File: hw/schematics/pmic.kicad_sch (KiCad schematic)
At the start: 40 parts, among them J1 TYPE-C-31-M-13C, J2 Conn_01x02, U1 NPM1300-QEAA-R

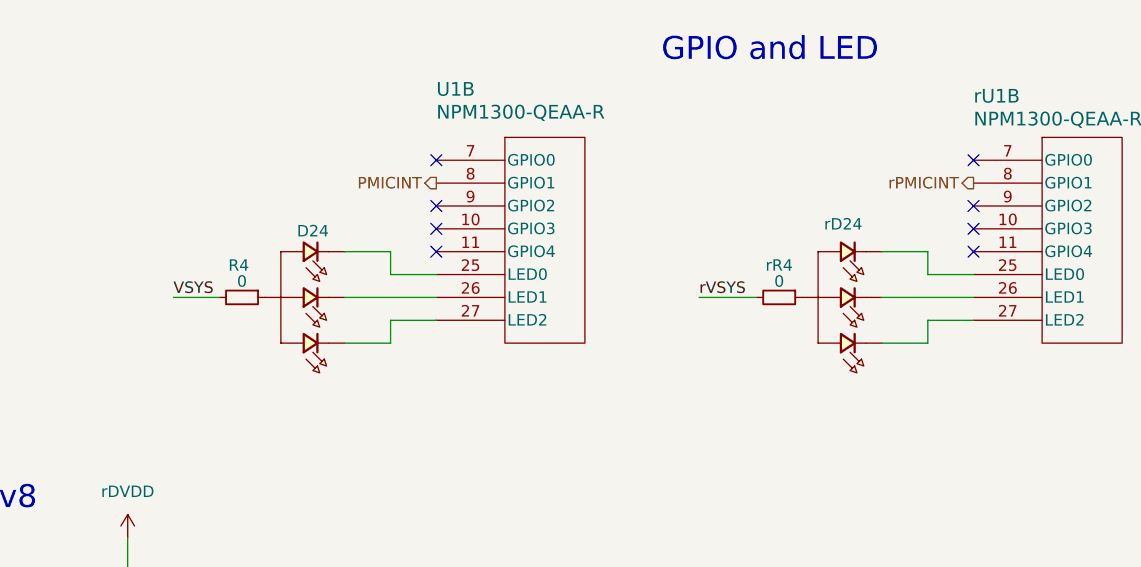
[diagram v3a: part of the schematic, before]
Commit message: Add extra pmic gpios
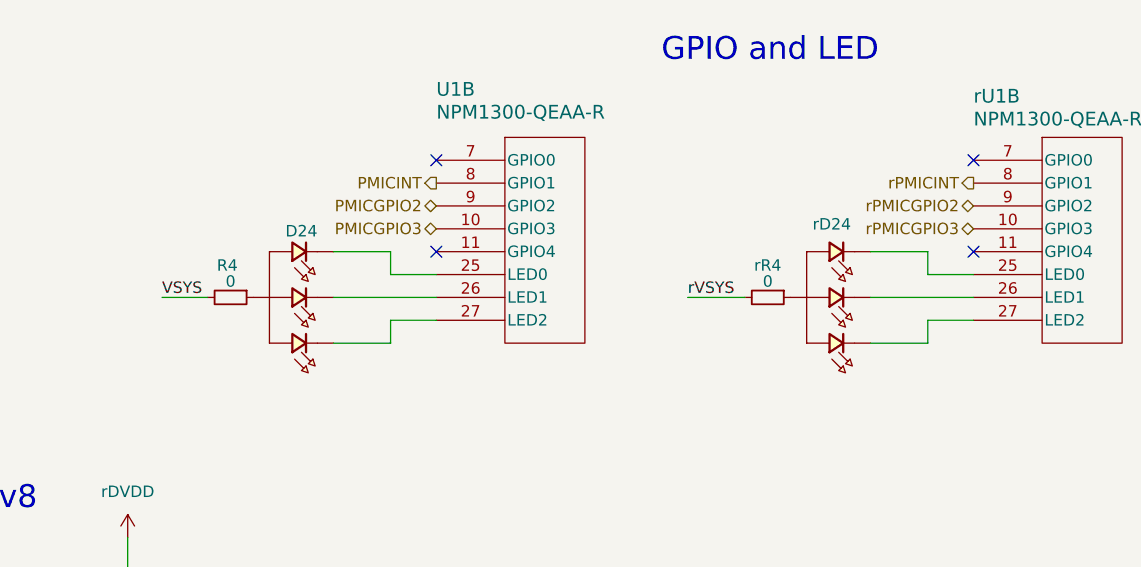
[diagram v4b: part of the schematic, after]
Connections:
- net PMICGPIO3: now reaches U1.10 (GPIO3)
- net PMICGPIO2: now reaches U1.9 (GPIO2)
- net rPMICGPIO3: now reaches rU1.10 (GPIO3)
- net rPMICGPIO2: now reaches rU1.9 (GPIO2)
- no-connect marks 28 -> 24
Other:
- moved on the sheet: D24, R4, rD24, rR4
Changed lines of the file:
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@@
 	)
 	(no_connect
-		(at 295.91 177.8)
-	)
-	(no_connect
 		(at 181.61 68.58)
 	)
@@
 	)
 	(no_connect
-		(at 295.91 175.26)
-	)
-	(no_connect
 		(at 181.61 60.96)
 	)
@@
 	)
 	(no_connect
-		(at 355.6 177.8)
-	)
-	(no_connect
-		(at 355.6 175.26)
-	)
-	(no_connect
 		(at 76.2 67.31)
 	)
@@
 	(wire
 		(pts
-			(xy 350.52 180.34) (xy 345.44 180.34)
+			(xy 350.52 180.34) (xy 344.17 180.34)
 		)
 		(stroke
@@
 	(wire
 		(pts
-			(xy 266.7 185.42) (xy 271.78 185.42)
+			(xy 265.43 185.42) (xy 270.51 185.42)
 		)
 		(stroke
@@
 	(wire
 		(pts
-			(xy 285.75 185.42) (xy 295.91 185.42)
+			(xy 284.48 185.42) (xy 295.91 185.42)
 		)
 		(stroke
@@
 	(wire
 		(pts
-			(xy 345.44 185.42) (xy 355.6 185.42)
+			(xy 344.17 185.42) (xy 355.6 185.42)
 		)
 		(stroke
@@
 	(wire
 		(pts
-			(xy 325.12 185.42) (xy 331.47 185.42)
+			(xy 323.85 185.42) (xy 330.2 185.42)
 		)
 		(stroke
@@
 	(wire
 		(pts
-			(xy 290.83 190.5) (xy 285.75 190.5)
+			(xy 290.83 190.5) (xy 284.48 190.5)
 		)
 		(stroke
@@
 	(wire
 		(pts
-			(xy 350.52 190.5) (xy 345.44 190.5)
+			(xy 350.52 190.5) (xy 344.17 190.5)
 		)
 		(stroke
@@
 	(wire
 		(pts
-			(xy 290.83 180.34) (xy 285.75 180.34)
+			(xy 290.83 180.34) (xy 284.48 180.34)
 		)
 		(stroke
@@
 	)
 	(label "VSYS"
-		(at 266.7 185.42 0)
+		(at 265.43 185.42 0)
 		(effects
 			(font
@@
 	)
 	(label "rVSYS"
-		(at 325.12 185.42 0)
+		(at 323.85 185.42 0)
 		(effects
 			(font
@@
 		)
 	)
+	(hierarchical_label "PMICGPIO2"
+		(shape bidirectional)
+		(at 295.91 175.26 180)
+		(effects
+			(font
+				(size 1.27 1.27)
+			)
+			(justify right)
+		)
+	)
 	(hierarchical_label "rPMICINT"
 		(shape output)
@@
 		)
 	)
+	(hierarchical_label "PMICGPIO3"
+		(shape bidirectional)
+		(at 295.91 177.8 180)
+		(effects
+			(font
+				(size 1.27 1.27)
+			)
+			(justify right)
+		)
+	)
 	(hierarchical_label "rSDA"
 		(shape bidirectional)
@@
 		)
 	)
+	(hierarchical_label "rPMICGPIO2"
+		(shape bidirectional)
+		(at 355.6 175.26 180)
+		(effects
+			(font
+				(size 1.27 1.27)
+			)
+			(justify right)
+		)
+	)
+	(hierarchical_label "rPMICGPIO3"
+		(shape bidirectional)
+		(at 355.6 177.8 180)
+		(effects
+			(font
+				(size 1.27 1.27)
+			)
+			(justify right)
+		)
+	)
 	(hierarchical_label "SCL"
 		(shape input)
@@
 	(symbol
 		(lib_id "Alidade:LED_RGB_COM_ANODE")
-		(at 341.63 185.42 0)
+		(at 340.36 185.42 0)
 		(mirror y)
 		(unit 1)
@@
 		(dnp no)
 		(property "Reference" "rD24"
-			(at 341.122 177.292 0)
+			(at 339.852 177.292 0)
 			(effects
 				(font
@@
 		)
 		(property "Value" "LED_RGB_COM_ANODE"
-			(at 340.995 176.53 0)
+			(at 339.725 176.53 0)
 			(effects
 				(font
@@
 		)
 		(property "Footprint" ""
-			(at 341.63 185.42 90)
+			(at 340.36 185.42 90)
 			(effects
 				(font
@@
 		)
 		(property "Datasheet" ""
-			(at 341.63 185.42 90)
+			(at 340.36 185.42 90)
 			(effects
 				(font
@@
 		)
 		(property "Description" ""
-			(at 341.63 185.42 0)
+			(at 340.36 185.42 0)
 			(effects
 				(font
@@
 	(symbol
 		(lib_id "Alidade:R")
-		(at 274.32 185.42 270)
+		(at 273.05 185.42 270)
 		(unit 1)
 		(exclude_from_sim no)
@@
 		(dnp no)
 		(property "Reference" "R4"
-			(at 272.796 181.864 90)
+			(at 271.526 181.864 90)
 			(effects
 				(font
@@
 		)
 		(property "Value" "0"
-			(at 274.32 183.642 90)
+			(at 273.05 183.642 90)
 			(do_not_autoplace yes)
 			(effects
@@
 		)
 		(property "Footprint" "Alidade:0603"
-			(at 274.32 185.42 0)
+			(at 273.05 185.42 0)
 			(effects
 				(font
@@
 		)
 		(property "Datasheet" ""
-			(at 274.32 185.42 0)
+			(at 273.05 185.42 0)
 			(effects
 				(font
@@
 		)
 		(property "Description" ""
-			(at 274.32 185.42 0)
+			(at 273.05 185.42 0)
 			(effects
 				(font
@@
 		)
 		(property "LCSC Part #" "C21189"
-			(at 274.32 185.42 90)
+			(at 273.05 185.42 90)
 			(effects
 				(font
@@
 	(symbol
 		(lib_id "Alidade:R")
-		(at 334.01 185.42 270)
+		(at 332.74 185.42 270)
 		(unit 1)
 		(exclude_from_sim no)
@@
 		(dnp no)
 		(property "Reference" "rR4"
-			(at 332.486 181.864 90)
+			(at 331.216 181.864 90)
 			(effects
 				(font
@@
 		)
 		(property "Value" "0"
-			(at 334.01 183.642 90)
+			(at 332.74 183.642 90)
 			(do_not_autoplace yes)
 			(effects
@@
 		)
 		(property "Footprint" "Alidade:0603"
-			(at 334.01 185.42 0)
+			(at 332.74 185.42 0)
 			(effects
 				(font
@@
 		)
 		(property "Datasheet" ""
-			(at 334.01 185.42 0)
+			(at 332.74 185.42 0)
 			(effects
 				(font
@@
 		)
 		(property "Description" ""
-			(at 334.01 185.42 0)
+			(at 332.74 185.42 0)
 			(effects
 				(font
@@
 		)
 		(property "LCSC Part #" "C21189"
-			(at 334.01 185.42 90)
+			(at 332.74 185.42 90)
 			(effects
 				(font
@@
 	(symbol
 		(lib_id "Alidade:LED_RGB_COM_ANODE")
-		(at 281.94 185.42 0)
+		(at 280.67 185.42 0)
 		(mirror y)
 		(unit 1)
@@
 		(dnp no)
 		(property "Reference" "D24"
-			(at 282.194 178.054 0)
+			(at 280.924 178.054 0)
 			(effects
 				(font
@@
 		)
 		(property "Value" "LED_RGB_COM_ANODE"
-			(at 281.305 176.53 0)
+			(at 280.035 176.53 0)
 			(effects
 				(font
@@
 		)
 		(property "Footprint" ""
-			(at 281.94 185.42 90)
+			(at 280.67 185.42 90)
 			(effects
 				(font
@@
 		)
 		(property "Datasheet" ""
-			(at 281.94 185.42 90)
+			(at 280.67 185.42 90)
 			(effects
 				(font
@@
 		)
 		(property "Description" ""
-			(at 281.94 185.42 0)
+			(at 280.67 185.42 0)
 			(effects
 				(font

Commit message: Add a bunch of models and footprints
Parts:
- C1, C2, C3, C4, C5, C6, C7, C8, rC1, rC2, rC3, rC4, rC5, rC6, rC7, rC8: footprint Alidade:0603 -> Alidade:C_0603_1608Metric
- L1, L2, rL1, rL2: footprint Alidade:0603 -> Alidade:L_0603_1608Metric
- R1, R2, R3, R4, R5, R6, rR1, rR2, rR3, rR4, rR5, rR6: footprint Alidade:0603 -> Alidade:R_0603_1608Metric
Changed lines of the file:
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@@
 			)
 		)
-		(property "Footprint" "Alidade:0603"
+		(property "Footprint" "Alidade:L_0603_1608Metric"
 			(at 43.18 143.51 0)
 			(effects
@@
 			)
 		)
-		(property "Footprint" "Alidade:0603"
+		(property "Footprint" "Alidade:R_0603_1608Metric"
 			(at 182.88 220.98 0)
 			(effects
@@
 			)
 		)
-		(property "Footprint" "Alidade:0603"
+		(property "Footprint" "Alidade:L_0603_1608Metric"
 			(at 138.43 147.32 0)
 			(effects
@@
 			)
 		)
-		(property "Footprint" "Alidade:0603"
+		(property "Footprint" "Alidade:C_0603_1608Metric"
 			(at 350.52 133.35 0)
 			(effects
@@
 			)
 		)
-		(property "Footprint" "Alidade:0603"
+		(property "Footprint" "Alidade:R_0603_1608Metric"
 			(at 356.87 69.85 0)
 			(effects
@@
 			)
 		)
-		(property "Footprint" "Alidade:0603"
+		(property "Footprint" "Alidade:C_0603_1608Metric"
 			(at 335.28 133.35 0)
 			(effects
@@
 			)
 		)
-		(property "Footprint" "Alidade:0603"
+		(property "Footprint" "Alidade:C_0603_1608Metric"
 			(at 279.4 133.35 0)
 			(effects
@@
 			)
 		)
-		(property "Footprint" "Alidade:0603"
+		(property "Footprint" "Alidade:C_0603_1608Metric"
 			(at 347.98 73.66 0)
 			(effects
@@
 			)
 		)
-		(property "Footprint" "Alidade:0603"
+		(property "Footprint" "Alidade:C_0603_1608Metric"
 			(at 264.16 133.35 0)
 			(effects
@@
 			)
 		)
-		(property "Footprint" "Alidade:0603"
+		(property "Footprint" "Alidade:C_0603_1608Metric"
 			(at 256.54 133.35 0)
 			(effects
@@
 			)
 		)
-		(property "Footprint" "Alidade:0603"
+		(property "Footprint" "Alidade:R_0603_1608Metric"
 			(at 285.75 68.58 0)
 			(effects
@@
 			)
 		)
-		(property "Footprint" "Alidade:0603"
+		(property "Footprint" "Alidade:R_0603_1608Metric"
 			(at 176.53 220.98 0)
 			(effects
@@
 			)
 		)
-		(property "Footprint" "Alidade:0603"
+		(property "Footprint" "Alidade:R_0603_1608Metric"
 			(at 142.24 153.67 0)
 			(effects
@@
 			)
 		)
-		(property "Footprint" "Alidade:0603"
+		(property "Footprint" "Alidade:R_0603_1608Metric"
 			(at 46.99 149.86 0)
 			(effects
@@
 			)
 		)
-		(property "Footprint" "Alidade:0603"
+		(property "Footprint" "Alidade:R_0603_1608Metric"
 			(at 273.05 185.42 0)
 			(effects
@@
 			)
 		)
-		(property "Footprint" "Alidade:0603"
+		(property "Footprint" "Alidade:R_0603_1608Metric"
 			(at 87.63 148.59 0)
 			(effects
@@
 			)
 		)
-		(property "Footprint" "Alidade:0603"
+		(property "Footprint" "Alidade:C_0603_1608Metric"
 			(at 81.28 60.96 0)
 			(effects
@@
 			)
 		)
-		(property "Footprint" "Alidade:0603"
+		(property "Footprint" "Alidade:C_0603_1608Metric"
 			(at 133.35 153.67 0)
 			(effects
@@
 			)
 		)
-		(property "Footprint" "Alidade:0603"
+		(property "Footprint" "Alidade:R_0603_1608Metric"
 			(at 250.19 222.25 0)
 			(effects
@@
 			)
 		)
-		(property "Footprint" "Alidade:0603"
+		(property "Footprint" "Alidade:L_0603_1608Metric"
 			(at 83.82 142.24 0)
 			(effects
@@
 			)
 		)
-		(property "Footprint" "Alidade:0603"
+		(property "Footprint" "Alidade:R_0603_1608Metric"
 			(at 332.74 185.42 0)
 			(effects
@@
 			)
 		)
-		(property "Footprint" "Alidade:0603"
+		(property "Footprint" "Alidade:C_0603_1608Metric"
 			(at 38.1 149.86 0)
 			(effects
@@
 			)
 		)
-		(property "Footprint" "Alidade:0603"
+		(property "Footprint" "Alidade:L_0603_1608Metric"
 			(at 181.61 146.05 0)
 			(effects
@@
 			)
 		)
-		(property "Footprint" "Alidade:0603"
+		(property "Footprint" "Alidade:C_0603_1608Metric"
 			(at 78.74 148.59 0)
 			(effects
@@
 			)
 		)
-		(property "Footprint" "Alidade:0603"
+		(property "Footprint" "Alidade:R_0603_1608Metric"
 			(at 256.54 222.25 0)
 			(effects
@@
 			)
 		)
-		(property "Footprint" "Alidade:0603"
+		(property "Footprint" "Alidade:C_0603_1608Metric"
 			(at 327.66 133.35 0)
 			(effects
@@
 			)
 		)
-		(property "Footprint" "Alidade:0603"
+		(property "Footprint" "Alidade:R_0603_1608Metric"
 			(at 185.42 152.4 0)
 			(effects
@@
 			)
 		)
-		(property "Footprint" "Alidade:0603"
+		(property "Footprint" "Alidade:C_0603_1608Metric"
 			(at 271.78 133.35 0)
 			(effects
@@
 			)
 		)
-		(property "Footprint" "Alidade:0603"
+		(property "Footprint" "Alidade:C_0603_1608Metric"
 			(at 176.53 152.4 0)
 			(effects
@@
 			)
 		)
-		(property "Footprint" "Alidade:0603"
+		(property "Footprint" "Alidade:C_0603_1608Metric"
 			(at 186.69 59.69 0)
 			(effects
@@
 			)
 		)
-		(property "Footprint" "Alidade:0603"
+		(property "Footprint" "Alidade:C_0603_1608Metric"
 			(at 342.9 133.35 0)
 			(effects
@@
 			)
 		)
-		(property "Footprint" "Alidade:0603"
+		(property "Footprint" "Alidade:C_0603_1608Metric"
 			(at 276.86 72.39 0)
 			(effects

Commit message: Various footprint updates
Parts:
- C1, C3, rC1, rC3: LCSC Part # C15849 -> (none)
- C2, rC2: LCSC Part # C23630 -> (none)
- C4, C5, C6, C7, C8, rC4, rC5, rC6, rC7, rC8: LCSC Part # C96446 -> (none)
- R1, R5, R6, rR1, rR5, rR6: LCSC Part # C25804 -> (none)
- R2, rR2: LCSC Part # C25819 -> (none)
- R3, R4, rR3, rR4: LCSC Part # C21189 -> (none)
- U1, rU1: footprint Alidade:QFN32_5X5_NOR -> Alidade:QFN32_5X5

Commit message: All footprints
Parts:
- D24, rD24: value LED_RGB_COM_ANODE -> 19-237/R6GHBHC-A01/2T; footprint (none) -> Alidade:19-237_R6GHBHC-A01_2T; LCSC Part # (none) -> C60105
- J2, rJ2: value Conn_01x02 -> S2B-PH-SM4-TB; footprint (none) -> Alidade:JST_S2B-PH-SM4-TB; LCSC Part # (none) -> C295747
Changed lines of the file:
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@@
 			)
 		)
-		(property "Value" "LED_RGB_COM_ANODE"
+		(property "Value" "19-237/R6GHBHC-A01/2T"
 			(at 339.725 176.53 0)
 			(effects
@@
 			)
 		)
-		(property "Footprint" ""
+		(property "Footprint" "Alidade:19-237_R6GHBHC-A01_2T"
 			(at 340.36 185.42 90)
 			(effects
@@
 			)
 		)
+		(property "LCSC Part #" "C60105"
+			(at 340.36 185.42 0)
+			(effects
+				(font
+					(size 1.27 1.27)
+				)
+				(hide yes)
+			)
+		)
 		(pin "3"
 		)
@@
 			)
 		)
-		(property "Value" "Conn_01x02"
+		(property "Value" "S2B-PH-SM4-TB"
 			(at 273.304 62.484 0)
 			(effects
@@
 			)
 		)
-		(property "Footprint" ""
+		(property "Footprint" "Alidade:JST_S2B-PH-SM4-TB"
 			(at 270.51 66.04 0)
 			(effects
@@
 			)
 		)
+		(property "LCSC Part #" "C295747"
+			(at 270.51 66.04 0)
+			(effects
+				(font
+					(size 1.27 1.27)
+				)
+				(hide yes)
+			)
+		)
 		(pin "2"
 		)
@@
 			)
 		)
-		(property "Value" "Conn_01x02"
+		(property "Value" "S2B-PH-SM4-TB"
 			(at 341.376 63.246 0)
 			(effects
@@
 			)
 		)
-		(property "Footprint" ""
+		(property "Footprint" "Alidade:JST_S2B-PH-SM4-TB"
 			(at 341.63 67.31 0)
 			(effects
@@
 			)
 		)
+		(property "LCSC Part #" "C295747"
+			(at 341.63 67.31 0)
+			(effects
+				(font
+					(size 1.27 1.27)
+				)
+				(hide yes)
+			)
+		)
 		(pin "1"
 		)
@@
 			)
 		)
-		(property "Value" "LED_RGB_COM_ANODE"
+		(property "Value" "19-237/R6GHBHC-A01/2T"
 			(at 280.035 176.53 0)
 			(effects
@@
 			)
 		)
-		(property "Footprint" ""
+		(property "Footprint" "Alidade:19-237_R6GHBHC-A01_2T"
 			(at 280.67 185.42 90)
 			(effects
@@
 			(at 280.67 185.42 0)
 			(effects
+				(font
+					(size 1.27 1.27)
+				)
+				(hide yes)
+			)
+		)
+		(property "LCSC Part #" "C60105"
+			(at 280.67 185.42 0)
+			(effects
